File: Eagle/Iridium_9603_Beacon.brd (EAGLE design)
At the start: 50.8 x 71.1 mm, 64 parts, among them J1 SS4-10-3.50-X-D, Q1 DMG3415U-7, U1 MCP111T-195I/TT, U2 SPX3819-3.3, U3 LTC3225EDDB#TRMPBF, U4 MPL3115A2LGA8, U5 ATSAMD21G18_QFN, U6 SAM-M8Q, X1 32.768

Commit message: Initial update for V4 - still work in progress
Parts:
- removed GND.: (no value), adafruit:1X01
- added C18: 10nF, microbuilder:0805-NO
- added C19: 10uF, microbuilder:0805-NO
- added CON4: uFL, microbuilder:U.FL
- added D4: MBR120, microbuilder:SOD-123
- added GND2, GND3, VBUS: (no value), adafruit:1X01
- added GNSS, IRIDIUM: SMA-142-0711-821/826, con-coax:J502-ND-142-0711-821/826
- added JP2: (no value), SparkFun-Passives:PAD-JUMPER-3-2OF3_NC_BY_TRACE_YES_SILK_LARGE
- added L1: 33nH, microbuilder:0805-NO
- added LED2: RED, microbuilder:CHIPLED_0805_NOOUTLINE
- added R10: 2.2K, microbuilder:0603-NO
- added R11: 30K, microbuilder:0805-NO
- added R9: 10 ohm, microbuilder:0805-NO
- added U7: LT1634-1,25BMCMS8, linear-technology:MSOP8
- BAT1, BAT2, BAT3: device SparkFun-Electromechanical:BATTERY-AAA-KEYSTONE82 -> SparkFun-Electromechanical:BATTERY-AAA-KEYSTONE92
- LED1: value RED -> (none); device microbuilder:CHIPLED_0805_NOOUTLINE -> SparkFun-LED:WS2812B
- R2: value 30K -> 12K
- R7: value 2.2K -> 47k
- U1: value MCP111T-195I/TT -> MCP111T-240E/TT
- U6: value SAM-M8Q -> MAX-M8; device ubloxLib:SAM-M8Q -> ubloxLib:MAX-M8
- moved SOLAR2+ 63.5 mm to (20.3, 63.5)
- moved SOLAR2- 61.9 mm to (37.2, 63.5)
- moved SWDIO 57.3 mm to (54.6, 18.7), turned to 90 degrees
- moved SWCLK 56.1 mm to (52.1, 18.7), turned to 90 degrees
- moved D2 37.9 mm to (21.6, 57.1), turned to 90 degrees
- moved BAT3 36.4 mm to (28.8, 8.73), turned to 180 degrees
- moved BAT1 24.2 mm to (28.8, 43.5), turned to 180 degrees
- moved D3 24.1 mm to (25.4, 57.2)
- moved SOLAR1+ 23.4 mm to (25.4, 63.5)
- moved BAT2 17.2 mm to (28.8, 26.1), turned to 0 degrees
- moved SOLAR1- 16.9 mm to (32.2, 63.5)
- moved D1 16.6 mm to (21.0, 53.1), turned to 180 degrees
- moved R7 16.4 mm to (35.4, 13.7), turned to 0 degrees
- moved FD2 9.64 mm to (52.5, 61.0)
- moved C6 9.31 mm to (18.2, 27.3), turned to 0 degrees
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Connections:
- new net 9_V_RESET_N: U6.9_RESET_N
- new net GPS_ANT: GNSS.1, L1.2, U6.11_RF_IN
- new net N$1: C18.1, L1.1, R9.1
- new net N$16: CON1.VBUS, D4.A
- new net N$17: JP2.3, R2.2
- new net N$18: JP2.1, R11.2
- new net N$3: LED2.A, R10.2
- new net VCC_RF: R9.2, U6.14_VCC_RF
- net +3V3: now also C19.1, LED1.1, U6.6_V_BCKP; no longer U6.3
- net 3V3SW: now also U6.7_VCC_IO, U6.8_VCC; no longer U6.17, U6.2
- net A0: now also R7.2, U7.6
- net D0: now also U6.2_TXD; no longer U6.13
- net D1: now also U6.3_RXD; no longer U6.14
- net D13: now also LED1.4, R10.1; no longer R7.1
- net GND: now also C18.2, C19.2, CON4.1, CON4.2, GND2.1, GND3.1, GNSS.G@1, GNSS.G@2, GNSS.G@3, GNSS.G@4, IRIDIUM.G@1, IRIDIUM.G@2, IRIDIUM.G@3, IRIDIUM.G@4, LED1.3, LED2.C, R11.1, U6.10_GND, U6.12_GND, U6.1_GND, U7.4; no longer GND..1, LED1.C, U6.1, U6.10, U6.11, U6.15, U6.16, U6.20, U6.4, U6.5, U6.6
- net N$11: now also JP2.2; no longer R2.2
- net N$2: now also CON4.3, IRIDIUM.1; no longer LED1.A, R7.2
- net VBUS: now also D4.C, R7.1, VBUS.1; no longer CON1.VBUS
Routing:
- net GND: track 633.8 -> 700.3 mm, vias 26 -> 15
- net A0: track 0.00 -> 35.7 mm, vias 0 -> 2
- net 3V3SW: track 71.1 -> 37.0 mm, vias 6 -> 2
- net N$14: track 21.5 -> 5.01 mm
- net SWCLK: track 41.6 -> 25.2 mm
- net D1: track 27.7 -> 41.5 mm
- net SWDIO: track 41.3 -> 27.7 mm
- net N$4: track 17.5 -> 4.47 mm
- net D0: track 28.2 -> 40.8 mm
- net N$11: track 4.29 -> 16.7 mm
- net VBAT: track 10.6 -> 22.8 mm, vias 0 -> 1
- net !RESET: track 24.5 -> 34.8 mm, vias 2 -> 4
- net N$1: track 0.00 -> 8.46 mm
- net +3V3: track 176.8 -> 184.2 mm, vias 12 -> 10
- net N$8: track 25.3 -> 32.6 mm
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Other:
- board size 50.8 x 71.1 mm -> 57.6 x 66 mm
- board text added: "150mA"
- board text added: "4.8V"
- board text added: "5.3V"
- board text added: "5.5V Max"
- board text added: "60mA"
- board text added: "Iridium 9603N Beacon V4"
- board text added: "Please return to:"
- board text removed: "Iridium 9603N Beacon V3"
- board text removed: "Please return to: Durham University ph-cfai-bit@durham.ac.uk"

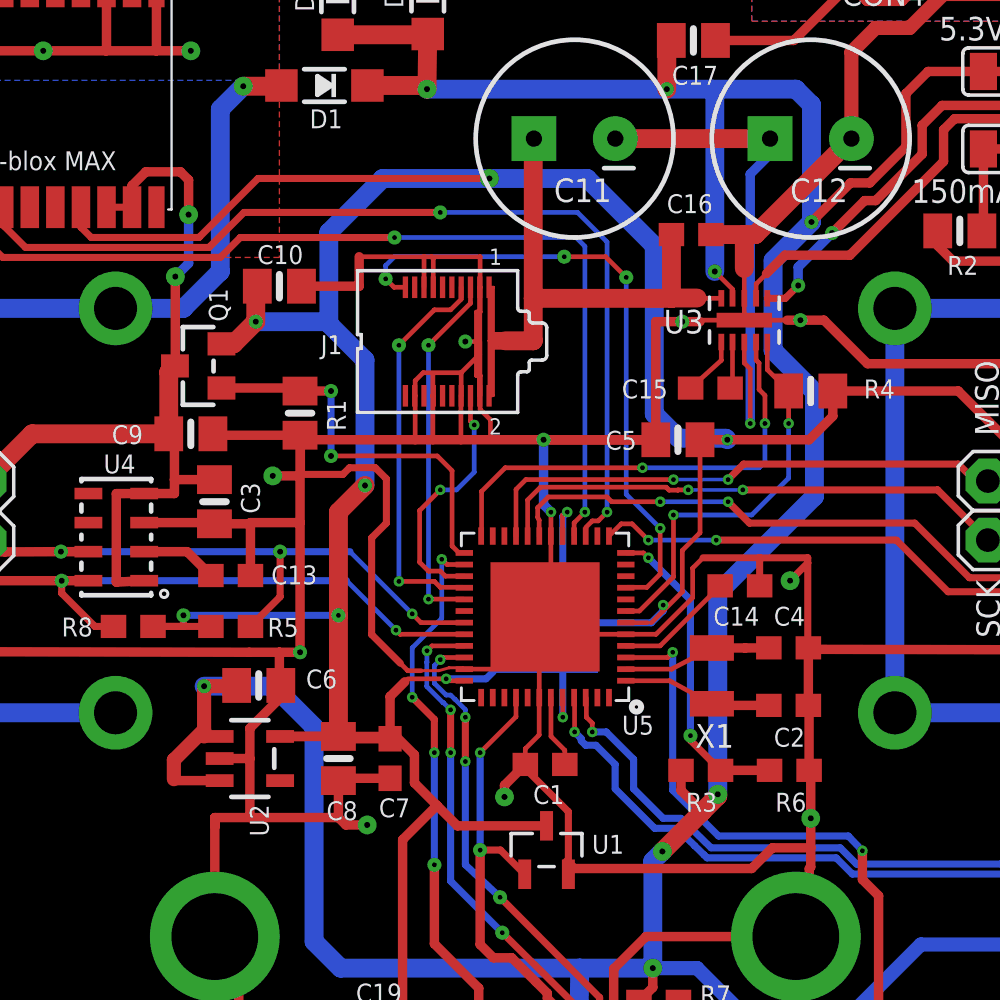
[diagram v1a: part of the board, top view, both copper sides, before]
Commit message: Included full details of RockBLOCK gateway messaging
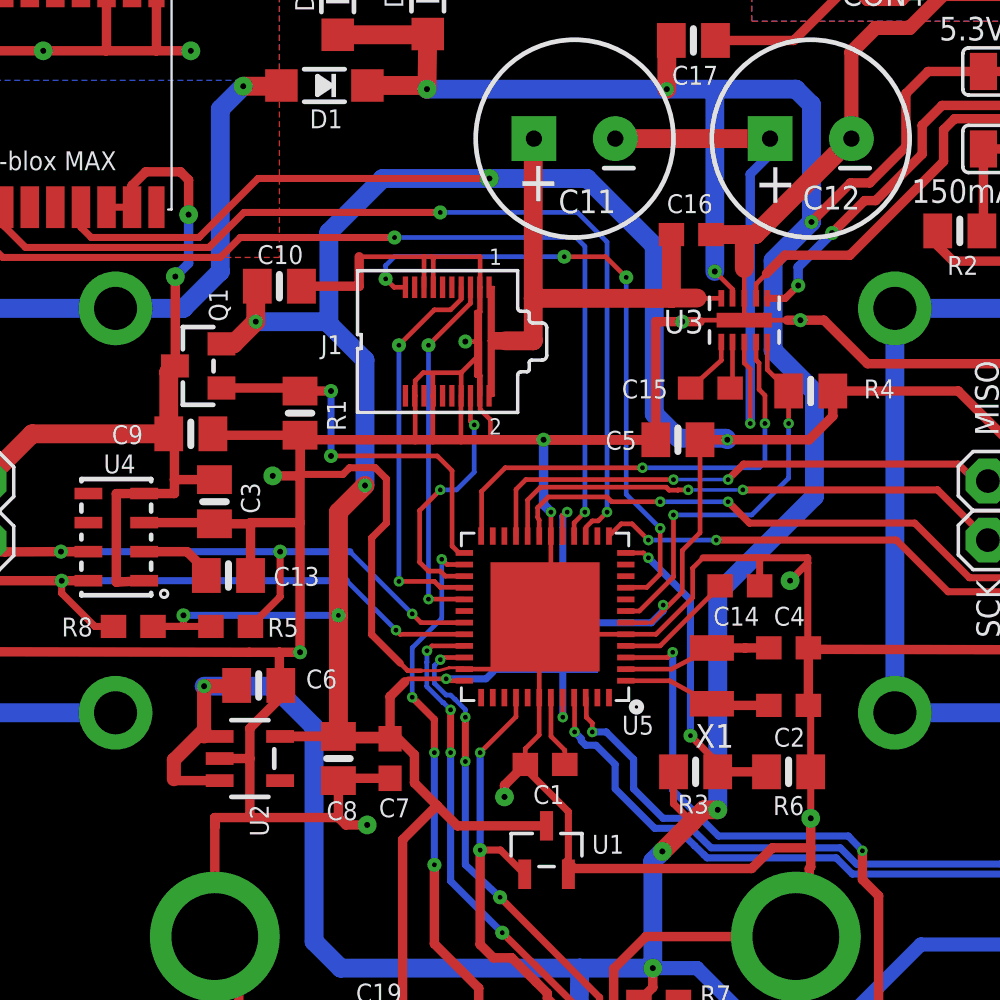
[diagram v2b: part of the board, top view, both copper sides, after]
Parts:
- C13, R6: device microbuilder:0603-NO -> microbuilder:0805-NO
- R3: value 100k -> 100K; device microbuilder:0603-NO -> microbuilder:0805-NO
- moved R3 0.23 mm to (37.0, 23.6), turned to 180 degrees
- moved C13 0.10 mm to (16.9, 32.0)
- moved R6 0.07 mm to (41.0, 23.6), turned to 180 degrees
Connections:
- net D9: now also R3.1, R6.2; no longer R3.2, R6.1
- net GND: now also R6.1; no longer R6.2
- net VBUS: now also R3.2; no longer R3.1
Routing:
- net VBUS: track 156.2 -> 156.9 mm
